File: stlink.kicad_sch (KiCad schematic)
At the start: 36 parts, among them Con4 USB_C_Wurth_632723300011, Q1 BC847B, U5 STM32F103C(8-B)Tx, U6 MCP1700T-3302E_MB, X1 8.000MHZ

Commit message: Corrected schematic
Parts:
- renumbered Con4 to CON4
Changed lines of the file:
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@@
   (symbol (lib_id "USB_Connectors:USB_C_Wurth_632723300011") (at 44.45 127 0) (unit 1)
     (in_bom yes) (on_board yes)
-    (property "Reference" "Con4" (id 0) (at 43.942 86.7368 0))
+    (property "Reference" "CON4" (id 0) (at 43.942 86.7368 0))
     (property "Value" "USB_C_Wurth_632723300011" (id 1) (at 45.212 89.0355 0))
     (property "Footprint" "Connector_USB:632723300011" (id 2) (at 45.72 124.46 0)

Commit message: Cleared all errors DRC
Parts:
- C26: symbol Capacitors_Smd1206:1nF_2kV_1206 -> Capacitors_Smd1206:1nF_2kV; Developer WP -> MW; LCSC Part #(optional) (none) -> C282813; Supplier TME -> Tme
- L6: Developer (none) -> MW; LCSC Part #(optional) (none) -> C76890; Manufacturer (none) -> MURATA; Manufacturer Part Number (none) -> BLM15HG601SN1D; Package (none) -> 0402; Price@1000pcs (none) -> 0,084; Price@1pc (none) -> 0,248; Supplier (none) -> Tme; Supplier Part Number (none) -> BLM15HG601SN1D; URL (none) -> https://www.tme.eu/pl/details/blm15hg601sn1d/ferryty-korali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
- Q1: LCSC Part #(optional) (none) -> C545561
- R10, R18, R20: LCSC Part #(optional) (none) -> C269684
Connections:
- net GND: now also CON4.SGND
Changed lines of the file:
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@@
+    (stroke (width 0) (type solid) (color 0 0 0 0))
+  )
+  (wire (pts (xy 24.13 152.4) (xy 21.59 152.4))
     (stroke (width 0) (type solid) (color 0 0 0 0))
   )
@@
   )
   (wire (pts (xy 66.04 97.79) (xy 66.04 99.06))
+    (stroke (width 0) (type solid) (color 0 0 0 0))
+  )
+  (wire (pts (xy 24.13 154.94) (xy 21.59 154.94))
     (stroke (width 0) (type solid) (color 0 0 0 0))
   )
@@
       (effects (font (size 7.62 7.62)) hide)
     )
-    (property "Datasheet" "C:/Wiktor/KiCad/KiCadWolowik/Schematic/Inductors/Components_Documentation/BLM15HG601SN1#.pdf" (id 3) (at 158.75 205.74 0)
+    (property "Datasheet" "https://www.tme.eu/Document/ea442a092e4ff19cd70ec3627ff4728b/BLM15HG601SN1%23.pdf" (id 3) (at 158.75 205.74 0)
       (effects (font (size 7.62 7.62)) hide)
+    )
+    (property "Manufacturer" "MURATA" (id 4) (at 173.99 193.04 0)
+      (effects (font (size 1.27 1.27)) hide)
+    )
+    (property "Manufacturer Part Number" "BLM15HG601SN1D" (id 5) (at 173.99 193.04 0)
+      (effects (font (size 1.27 1.27)) hide)
+    )
+    (property "Supplier" "Tme" (id 6) (at 173.99 193.04 0)
+      (effects (font (size 1.27 1.27)) hide)
+    )
+    (property "Supplier Part Number" "BLM15HG601SN1D " (id 7) (at 173.99 193.04 0)
+      (effects (font (size 1.27 1.27)) hide)
+    )
+    (property "URL" "https://www.tme.eu/pl/details/blm15hg601sn1d/ferryty-koraliki/murata/" (id 8) (at 173.99 193.04 0)
+      (effects (font (size 1.27 1.27)) hide)
+    )
+    (property "Price@1pc" "0,248" (id 9) (at 173.99 193.04 0)
+      (effects (font (size 1.27 1.27)) hide)
+    )
+    (property "Price@1000pcs" "0,084" (id 10) (at 173.99 193.04 0)
+      (effects (font (size 1.27 1.27)) hide)
+    )
+    (property "Developer" "MW" (id 11) (at 173.99 193.04 0)
+      (effects (font (size 1.27 1.27)) hide)
+    )
+    (property "Package" "0402" (id 12) (at 173.99 193.04 0)
+      (effects (font (size 1.27 1.27)) hide)
+    )
+    (property "LCSC Part #(optional)" "C76890" (id 13) (at 173.99 193.04 0)
+      (effects (font (size 1.27 1.27)) hide)
     )
     (pin "1")
@@
       (effects (font (size 1.27 1.27)) hide)
     )
+    (property "LCSC Part #(optional)" "C269684" (id 13) (at 172.72 132.08 0)
+      (effects (font (size 1.27 1.27)) hide)
+    )
     (pin "1")
     (pin "2")
@@
       (effects (font (size 1.27 1.27)) hide)
     )
+    (property "LCSC Part #(optional)" "C269684" (id 13) (at 162.56 134.62 0)
+      (effects (font (size 1.27 1.27)) hide)
+    )
     (pin "1")
     (pin "2")
@@
     (pin "1")
   )
-  (symbol (lib_id "Capacitors_Smd1206:1nF_2kV_1206") (at 36.83 179.07 180) (unit 1)
+  (symbol (lib_id "Capacitors_Smd1206:1nF_2kV") (at 36.83 179.07 180) (unit 1)
     (in_bom yes) (on_board yes)
     (property "Reference" "C26" (id 0) (at 41.91 177.8 0))
@@
       (effects (font (size 1.27 1.27)) hide)
     )
-    (property "Datasheet" "Capacitors/Smd_1206/Components_Documentation/1nF_2kV_1206.pdf" (id 3) (at 41.91 181.61 0)
+    (property "Datasheet" "https://www.tme.eu/Document/fbb9415081fcefba62c0f8bbf5b21210/UPY-GPHC_X7R_6.3V-to-50V_20.pdf" (id 3) (at 41.91 181.61 0)
       (effects (font (size 1.27 1.27)) hide)
     )
@@
       (effects (font (size 1.27 1.27)) hide)
     )
-    (property "Supplier" "TME" (id 6) (at 36.83 179.07 0)
+    (property "Supplier" "Tme" (id 6) (at 36.83 179.07 0)
       (effects (font (size 1.27 1.27)) hide)
     )
@@
       (effects (font (size 1.27 1.27)) hide)
     )
-    (property "Developer" "WP" (id 11) (at 36.83 179.07 0)
+    (property "Developer" "MW" (id 11) (at 36.83 179.07 0)
       (effects (font (size 1.27 1.27)) hide)
     )
     (property "Package" "1206" (id 12) (at 36.83 179.07 0)
+      (effects (font (size 1.27 1.27)) hide)
+    )
+    (property "LCSC Part #(optional)" "C282813" (id 13) (at 36.83 179.07 0)
       (effects (font (size 1.27 1.27)) hide)
     )
@@
       (effects (font (size 1.524 1.524)) hide)
     )
-    (property "Datasheet" "Transistors/Bipolar/Components_Documentation/BC84x(6_7).pdf" (id 3) (at 107.95 140.97 0)
+    (property "Datasheet" "https://www.tme.eu/Document/6f1446946b61c6ee994e420fd75b3124/bc847_8_9_bc850.pdf" (id 3) (at 107.95 140.97 0)
       (effects (font (size 1.524 1.524)) hide)
     )
@@
     )
     (property "Package" "SOT23-3" (id 11) (at 107.95 140.97 0)
+      (effects (font (size 1.27 1.27)) hide)
+    )
+    (property "LCSC Part #(optional)" "C545561" (id 12) (at 107.95 140.97 0)
       (effects (font (size 1.27 1.27)) hide)
     )
@@
       (effects (font (size 1.27 1.27)) hide)
     )
+    (property "LCSC Part #(optional)" "C269684" (id 13) (at 97.79 148.59 0)
+      (effects (font (size 1.27 1.27)) hide)
+    )
     (pin "1")
     (pin "2")
@@
     (pin "1")
   )
+  (symbol (lib_id "power:GND") (at 21.59 154.94 270) (unit 1)
+    (in_bom yes) (on_board yes)
+    (property "Reference" "#PWR0229" (id 0) (at 24.13 154.94 0)
+      (effects (font (size 0.762 0.762)) hide)
+    )
+    (property "Value" "GND" (id 1) (at 19.05 154.94 0)
+      (effects (font (size 0.762 0.762)) hide)
+    )
+    (property "Footprint" "" (id 2) (at 21.59 154.94 0)
+      (effects (font (size 1.524 1.524)))
+    )
+    (property "Datasheet" "" (id 3) (at 21.59 154.94 0)
+      (effects (font (size 1.524 1.524)))
+    )
+    (pin "1")
+  )
   (symbol (lib_id "USB_Connectors:USB_C_Wurth_632723300011") (at 44.45 127 0) (unit 1)
     (in_bom yes) (on_board yes)
@@
       (effects (font (size 1.27 1.27)) hide)
     )
+    (property "LCSC Part #(optional)" "" (id 13) (at 44.45 127 0))
     (pin "A1")
     (pin "A10")
@@
     (pin "S3")
     (pin "S4")
+    (pin "SGND")
+    (pin "SGND")
+  )
+  (symbol (lib_id "power:GND") (at 21.59 152.4 270) (unit 1)
+    (in_bom yes) (on_board yes)
+    (property "Reference" "#PWR0228" (id 0) (at 24.13 152.4 0)
+      (effects (font (size 0.762 0.762)) hide)
+    )
+    (property "Value" "GND" (id 1) (at 19.05 152.4 0)
+      (effects (font (size 0.762 0.762)) hide)
+    )
+    (property "Footprint" "" (id 2) (at 21.59 152.4 0)
+      (effects (font (size 1.524 1.524)))
+    )
+    (property "Datasheet" "" (id 3) (at 21.59 152.4 0)
+      (effects (font (size 1.524 1.524)))
+    )
+    (pin "1")
   )
 )

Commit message: Eliminated all warnings realted with footprints
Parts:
- C22, C23, C24, C25, C27, C28, C29: footprint Capacitors_Smd_0603:100nF_0603 -> Capacitors_Smd_0402:100nF_0402; symbol Capacitors_Smd0603:100n -> Capacitors_Smd0402:100nF; Developer (none) -> MW; LCSC Part # (optional) (none) -> C131394; Manufacturer SAMSUNG -> Murata; Manufacturer Part Number CL10B104JB8NNNC -> GRM155R71H104KE14D; Package 0603 -> 0402; Package_1 (none) -> 0402; Price@1000pcs 0,02231 -> 0,03299; Price@1pc 0,04540 -> 0,07091; Supplier TME -> Tme; Supplier Part Number CL10B104JB8NNNC -> GRM155R71H104KE14D; URL https://www.tme.eu/pl/details/cl10b104jb8nnnc/kondensatory-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 -> https://www.tme.eu/pl/details/grm155r71h104ke14d/kondensato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

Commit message: Gerbers created, BOM, CPL
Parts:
- removed C21, C30: 10uF/6V3, Capacitors_Smd_0805:10uF_0805, symbol Capacitors_Smd0805:10uF_6V3
- added C21, C30: 10uF/6.3V, Capacitors_Smd_0603:10uF_10V_0603, symbol Capacitors_Smd0603:10uF
- C27: value 100n/50V -> 100nF/50V
- R21, R9: Price@1pcs (none) -> 0,07415
- U6: Developer WP -> MW; LCSC Part #(optional) (none) -> C632000; Package (none) -> SOT89
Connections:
- net 3V3: now also C21.1, C30.1
- net GND: now also C21.2, C30.2

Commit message: New branch created
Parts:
- removed D2: BAT54C, Diodes:BAT54C, symbol Diodes:BAT54C
- added D12, D2: (no value), symbol Diodes:PMEG2015EA
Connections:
- net 5V: no longer CON4.A4 (VBUS), CON4.A9 (VBUS_1), CON4.B4 (VBUS_2), CON4.B9 (VBUS_3)
- net POWER_IN_5V: now also D2.2 (A)
- net at C28.1, U6.2 (Vin): now also D12.1 (K), D2.1 (K)
- new net: CON4.A4 (VBUS), CON4.A9 (VBUS_1), CON4.B4 (VBUS_2), CON4.B9 (VBUS_3), D12.2 (A)
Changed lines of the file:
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@@
   (junction (at 36.83 171.45) (diameter 1.016) (color 0 0 0 0)
   )
-  (junction (at 74.93 97.79) (diameter 1.016) (color 0 0 0 0)
-  )
   (junction (at 127 185.42) (diameter 1.016) (color 0 0 0 0)
   )
@@
   )
   (junction (at 138.43 82.55) (diameter 1.016) (color 0 0 0 0)
+  )
+  (junction (at 90.17 82.55) (diameter 0) (color 0 0 0 0)
   )
   (junction (at 35.56 171.45) (diameter 1.016) (color 0 0 0 0)
@@
     (stroke (width 0) (type solid) (color 0 0 0 0))
   )
-  (wire (pts (xy 77.47 97.79) (xy 74.93 97.79))
-    (stroke (width 0) (type solid) (color 0 0 0 0))
-  )
   (wire (pts (xy 125.73 82.55) (xy 138.43 82.55))
     (stroke (width 0) (type solid) (color 0 0 0 0))
@@
     (stroke (width 0) (type solid) (color 0 0 0 0))
   )
+  (wire (pts (xy 87.63 80.01) (xy 90.17 80.01))
+    (stroke (width 0) (type default) (color 0 0 0 0))
+  )
   (wire (pts (xy 152.4 200.66) (xy 152.4 198.12))
     (stroke (width 0) (type solid) (color 0 0 0 0))
   )
+  (wire (pts (xy 90.17 80.01) (xy 90.17 82.55))
+    (stroke (width 0) (type default) (color 0 0 0 0))
+  )
   (wire (pts (xy 379.73 134.62) (xy 379.73 143.51))
     (stroke (width 0) (type solid) (color 0 0 0 0))
@@
     (stroke (width 0) (type solid) (color 0 0 0 0))
   )
+  (wire (pts (xy 87.63 85.09) (xy 90.17 85.09))
+    (stroke (width 0) (type default) (color 0 0 0 0))
+  )
   (wire (pts (xy 401.32 123.19) (xy 398.78 123.19))
     (stroke (width 0) (type solid) (color 0 0 0 0))
@@
   (wire (pts (xy 114.3 185.42) (xy 101.6 185.42))
     (stroke (width 0) (type solid) (color 0 0 0 0))
+  )
+  (wire (pts (xy 90.17 85.09) (xy 90.17 82.55))
+    (stroke (width 0) (type default) (color 0 0 0 0))
   )
   (wire (pts (xy 114.3 200.66) (xy 114.3 198.12))
@@
     (pin "1")
   )
-  (symbol (lib_id "Diodes:BAT54C") (at 82.55 82.55 270) (unit 1)
-    (in_bom yes) (on_board yes)
-    (property "Reference" "D2" (id 0) (at 83.82 74.549 90))
-    (property "Value" "BAT54C" (id 1) (at 83.82 76.8604 90))
-    (property "Footprint" "Diodes:BAT54C" (id 2) (at 82.55 82.55 0)
-      (effects (font (size 1.27 1.27)) hide)
-    )
-    (property "Datasheet" "https://www.tme.eu/Document/d38616c6cb165f21e555b4db7b25411b/BAT54_SERIES.pdf" (id 3) (at 82.55 82.55 0)
-      (effects (font (size 1.27 1.27)) hide)
-    )
-    (property "Manufacturer" "Nexperia" (id 4) (at 82.55 82.55 0)
-      (effects (font (size 1.27 1.27)) hide)
-    )
-    (property "Manufacturer Part Number" "BAT54C.215" (id 5) (at 82.55 82.55 0)
-      (effects (font (size 1.27 1.27)) hide)
-    )
-    (property "Supplier" "Tme" (id 6) (at 82.55 82.55 0)
-      (effects (font (size 1.27 1.27)) hide)
-    )
-    (property "Supplier Part Number" "BAT54C" (id 7) (at 82.55 82.55 0)
-      (effects (font (size 1.27 1.27)) hide)
-    )
-    (property "URL" "https://www.tme.eu/pl/details/bat54c/diody-schottky-smd/nexperia/bat54c-215/" (id 8) (at 82.55 82.55 0)
-      (effects (font (size 1.27 1.27)) hide)
-    )
-    (property "Price@1pc" "0,15864" (id 9) (at 82.55 82.55 0)
-      (effects (font (size 1.27 1.27)) hide)
-    )
-    (property "Price@1000pcs" "0,07" (id 10) (at 82.55 82.55 0)
-      (effects (font (size 1.27 1.27)) hide)
-    )
-    (property "Developer" "MW" (id 11) (at 82.55 82.55 0)
-      (effects (font (size 1.27 1.27)) hide)
-    )
-    (property "Package" "Sot23-3" (id 12) (at 82.55 82.55 0)
-      (effects (font (size 1.27 1.27)) hide)
-    )
-    (property "LCSC Part #(optional)" "C369922" (id 13) (at 82.55 82.55 0)
-      (effects (font (size 1.27 1.27)) hide)
-    )
-    (pin "1")
-    (pin "2")
-    (pin "3")
-  )
   (symbol (lib_id "power:GND_NO_GLOBAL") (at 77.47 76.2 270) (unit 1)
     (in_bom yes) (on_board yes)
@@
     )
     (property "Datasheet" "" (id 3) (at 100.33 138.43 0)
-      (effects (font (size 1.524 1.524)))
-    )
-    (pin "1")
-  )
-  (symbol (lib_id "power:5V_NO_GLOBAL") (at 77.47 97.79 270) (unit 1)
-    (in_bom yes) (on_board yes)
-    (property "Reference" "#PWR45" (id 0) (at 77.47 96.52 90)
-      (effects (font (size 0.508 0.508)) hide)
-    )
-    (property "Value" "5V" (id 1) (at 80.7212 97.8154 90)
-      (effects (font (size 1.27 1.27)) (justify left))
-    )
-    (property "Footprint" "" (id 2) (at 77.47 97.79 0)
-      (effects (font (size 1.524 1.524)))
-    )
-    (property "Datasheet" "" (id 3) (at 77.47 97.79 0)
       (effects (font (size 1.524 1.524)))
     )
@@
     (pin "1")
   )
+  (symbol (lib_id "Diodes:PMEG2015EA") (at 82.55 80.01 0) (unit 1)
+    (in_bom yes) (on_board yes)
+    (property "Reference" "D2" (id 0) (at 80.01 75.565 0))
+    (property "Value" "" (id 1) (at 87.63 77.47 0))
+    (property "Footprint" "" (id 2) (at 87.63 95.25 0)
+      (effects (font (size 1.27 1.27)) hide)
+    )
+    (property "Datasheet" "https://pl.mouser.com/datasheet/2/916/PMEG2015EA-1599826.pdf" (id 3) (at 87.63 95.25 0)
+      (effects (font (size 1.27 1.27)) hide)
+    )
+    (property "Manufacturer" "Nexperia" (id 4) (at 82.55 80.01 0)
+      (effects (font (size 1.27 1.27)) hide)
+    )
+    (property "Manufacturer Part Number" "PMEG2015EA,115" (id 5) (at 82.55 80.01 0)
+      (effects (font (size 1.27 1.27)) hide)
+    )
+    (property "Supplier" "Mouser" (id 6) (at 82.55 80.01 0)
+      (effects (font (size 1.27 1.27)) hide)
+    )
+    (property "Supplier Part Number" "771-PMEG2015EA115" (id 7) (at 82.55 80.01 0)
+      (effects (font (size 1.27 1.27)) hide)
+    )
+    (property "URL" "https://pl.mouser.com/ProductDetail/Nexperia/PMEG2015EA115?qs=LOCUfHb8d9uL8QMkobJwRA%3D%3D" (id 8) (at 82.55 80.01 0)
+      (effects (font (size 1.27 1.27)) hide)
+    )
+    (property "Price@1pc" "1,40" (id 9) (at 82.55 80.01 0)
+      (effects (font (size 1.27 1.27)) hide)
+    )
+    (property "Price@1000pcs" "0,432" (id 10) (at 82.55 80.01 0)
+      (effects (font (size 1.27 1.27)) hide)
+    )
+    (property "Developer" "WP" (id 11) (at 82.55 80.01 0)
+      (effects (font (size 1.27 1.27)) hide)
+    )
+    (property "Package" "SOD-323" (id 12) (at 82.55 80.01 0)
+      (effects (font (size 1.27 1.27)) hide)
+    )
+    (property "LCSC Part #(optional)" "C552831" (id 13) (at 82.55 80.01 0)
+      (effects (font (size 1.27 1.27)) hide)
+    )
+    (pin "1")
+    (pin "2")
+  )
+  (symbol (lib_id "Diodes:PMEG2015EA") (at 82.55 85.09 0) (unit 1)
+    (in_bom yes) (on_board yes)
+    (property "Reference" "D12" (id 0) (at 78.74 83.82 0))
+    (property "Value" "" (id 1) (at 82.55 88.265 0))
+    (property "Footprint" "" (id 2) (at 87.63 100.33 0)
+      (effects (font (size 1.27 1.27)) hide)
+    )
+    (property "Datasheet" "https://pl.mouser.com/datasheet/2/916/PMEG2015EA-1599826.pdf" (id 3) (at 87.63 100.33 0)
+      (effects (font (size 1.27 1.27)) hide)
+    )
+    (property "Manufacturer" "Nexperia" (id 4) (at 82.55 85.09 0)
+      (effects (font (size 1.27 1.27)) hide)
+    )
+    (property "Manufacturer Part Number" "PMEG2015EA,115" (id 5) (at 82.55 85.09 0)
+      (effects (font (size 1.27 1.27)) hide)
+    )
+    (property "Supplier" "Mouser" (id 6) (at 82.55 85.09 0)
+      (effects (font (size 1.27 1.27)) hide)
+    )
+    (property "Supplier Part Number" "771-PMEG2015EA115" (id 7) (at 82.55 85.09 0)
+      (effects (font (size 1.27 1.27)) hide)
+    )
+    (property "URL" "https://pl.mouser.com/ProductDetail/Nexperia/PMEG2015EA115?qs=LOCUfHb8d9uL8QMkobJwRA%3D%3D" (id 8) (at 82.55 85.09 0)
+      (effects (font (size 1.27 1.27)) hide)
+    )
+    (property "Price@1pc" "1,40" (id 9) (at 82.55 85.09 0)
+      (effects (font (size 1.27 1.27)) hide)
+    )
+    (property "Price@1000pcs" "0,432" (id 10) (at 82.55 85.09 0)
+      (effects (font (size 1.27 1.27)) hide)
+    )
+    (property "Developer" "WP" (id 11) (at 82.55 85.09 0)
+      (effects (font (size 1.27 1.27)) hide)
+    )
+    (property "Package" "SOD-323" (id 12) (at 82.55 85.09 0)
+      (effects (font (size 1.27 1.27)) hide)
+    )
+    (property "LCSC Part #(optional)" "C552831" (id 13) (at 82.55 85.09 0)
+      (effects (font (size 1.27 1.27)) hide)
+    )
+    (pin "1")
+    (pin "2")
+  )
   (symbol (lib_id "USB_Connectors:USB_C_Wurth_632723300011") (at 44.45 127 0) (unit 1)

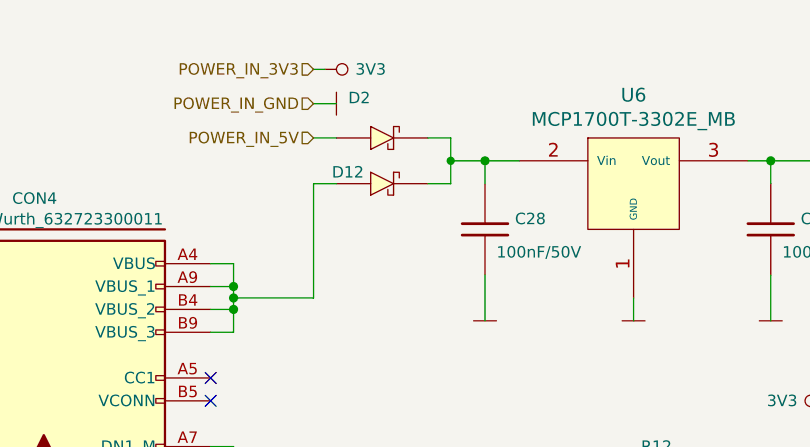
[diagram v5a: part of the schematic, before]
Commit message: Changed ethernet connector to horizontal and changed it position to avoid collision with arduino shield
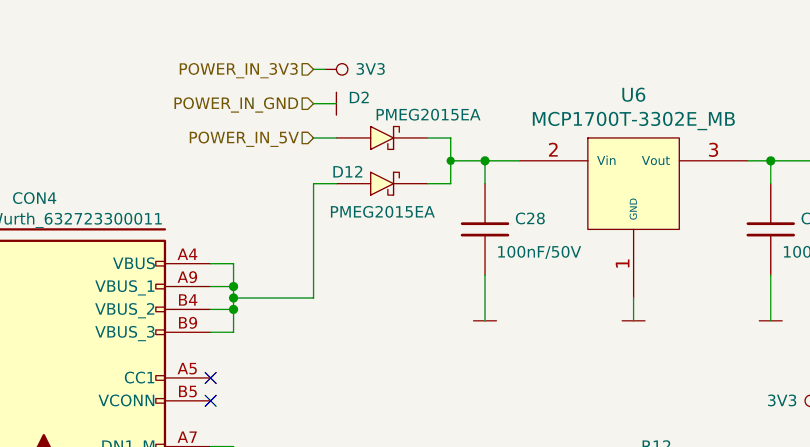
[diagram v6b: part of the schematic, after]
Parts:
- D12, D2: value (none) -> PMEG2015EA; footprint (none) -> Diodes:PMEG2015EA
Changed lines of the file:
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@@
     (in_bom yes) (on_board yes)
     (property "Reference" "D2" (id 0) (at 80.01 75.565 0))
-    (property "Value" "" (id 1) (at 87.63 77.47 0))
-    (property "Footprint" "" (id 2) (at 87.63 95.25 0)
+    (property "Value" "PMEG2015EA" (id 1) (at 87.63 77.47 0))
+    (property "Footprint" "Diodes:PMEG2015EA" (id 2) (at 87.63 95.25 0)
       (effects (font (size 1.27 1.27)) hide)
     )
@@
     (in_bom yes) (on_board yes)
     (property "Reference" "D12" (id 0) (at 78.74 83.82 0))
-    (property "Value" "" (id 1) (at 82.55 88.265 0))
-    (property "Footprint" "" (id 2) (at 87.63 100.33 0)
+    (property "Value" "PMEG2015EA" (id 1) (at 82.55 88.265 0))
+    (property "Footprint" "Diodes:PMEG2015EA" (id 2) (at 87.63 100.33 0)
       (effects (font (size 1.27 1.27)) hide)
     )
